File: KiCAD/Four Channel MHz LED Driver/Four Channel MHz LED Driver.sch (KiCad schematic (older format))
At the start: 15 parts

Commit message: Simpler power supply
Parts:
- removed C? (x2): 4.7uF, Capacitor_SMD:C_0805_2012Metric, symbol Device:C_Small
- removed C? (x3): 47uF, Capacitor_SMD:C_1206_3216Metric, symbol Device:C_Small
- removed C? (x2): 1uF, Capacitor_SMD:C_0603_1608Metric, symbol Device:C_Small
- removed C?: 100uF, Capacitor_SMD:C_1206_3216Metric, symbol Device:C_Small
- removed R? (x2): 100k, Resistor_SMD:R_0603_1608Metric, symbol Device:R_Small
- removed R?: 130k, Resistor_SMD:R_0603_1608Metric, symbol Device:R_Small
- removed R?: 60.4k, Resistor_SMD:R_0603_1608Metric, symbol Device:R_Small
- removed U?: LTM8049IY, LTM8049IY_ADI, symbol Custom_parts:LTM8049IY
- added C? (x4): 47uF, Capacitor_SMD:C_1206_3216Metric, symbol Device:C_Small
- added C? (x2): 1500pF, Capacitor_SMD:C_0603_1608Metric, symbol Device:C_Small
- added C? (x4): 2.2uF, Custom Footprints:0508_Capacitor, symbol Device:C_Small
- added L?: 10uH, Inductor_SMD:L_1210_3225Metric, symbol pspice:INDUCTOR
- added R?: 100, Resistor_SMD:R_0805_2012Metric, symbol Device:R_Small
- added U?: S18V20F12_12V_DC, symbol Custom_parts:S18V20F12_12V_DC
- added U?: DPBW06F-05, Custom Footprints:DPBW06F-05, symbol Custom_parts:DPBW06F-05
- added U?: ADP7118AUJZ-5.0-R7, Custom Footprints:ADP7118AUJZ-R7, symbol Custom_parts:ADP7118AUJZ-5.0-R7
- U?: footprint MUB10A_TEX -> Custom Footprints:DAC084S085CIMM
- U?: footprint TSSOP20_MC_MCH -> Custom Footprints:MCP4351-502E
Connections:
- net labels added: 5V-analog
- net labels removed: PS_Monitor
- wire segments 46 -> 54
- no-connect marks 5 -> 3
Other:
- note added: "ISOLATED - 12V to split +/- 5V"
- note added: "LDO - 12V to clean 5V for analog circuits"
- note added: "SEPIC - Vin (3V - 30V) to 12V DC"

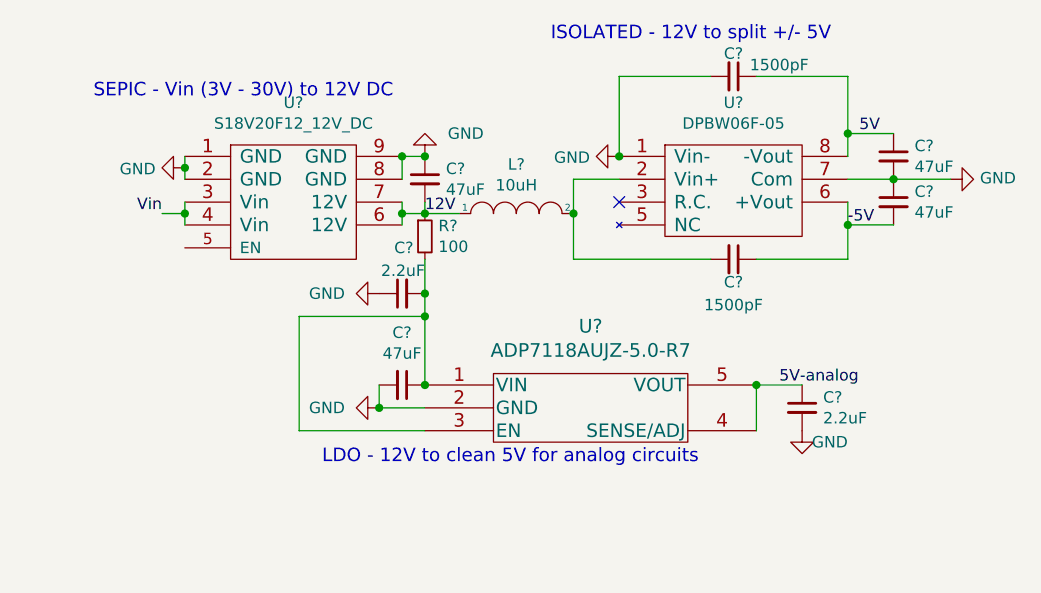
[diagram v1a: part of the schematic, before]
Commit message: Add Spice models
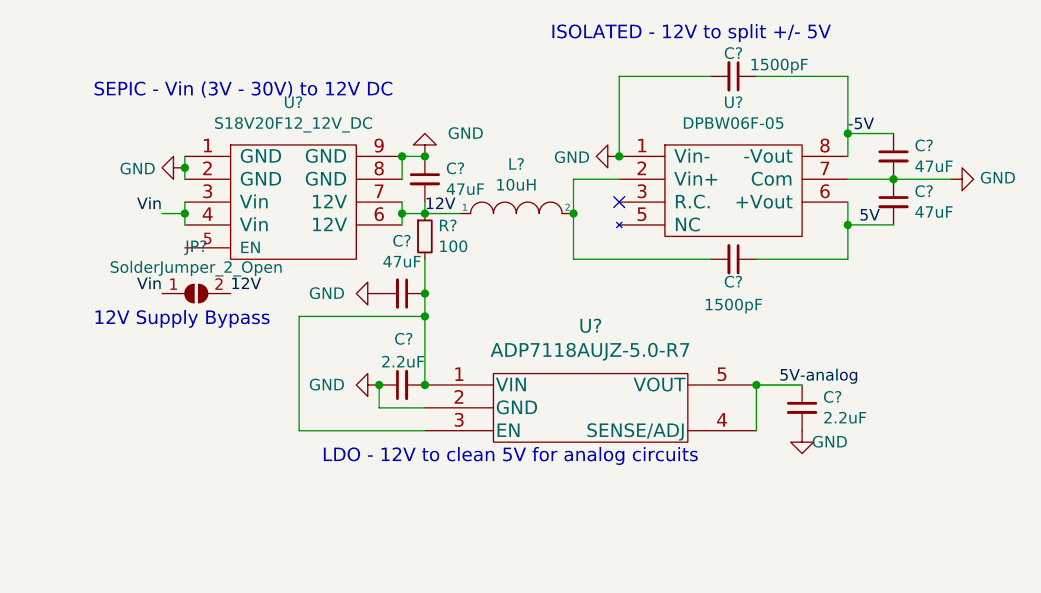
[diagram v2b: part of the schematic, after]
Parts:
- removed C?: 47uF, Capacitor_SMD:C_1206_3216Metric, symbol Device:C_Small
- added C?: 47uF, Capacitor_SMD:C_1206_3216Metric, symbol Device:C_Small
- added JP?: SolderJumper_2_Open, Jumper:SolderJumper-2_P1.3mm_Open_Pad1.0x1.5mm, symbol Jumper:SolderJumper_2_Open
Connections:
- net -5V: now also C?.1, C?.1, U?.8 (-Vout); no longer C?.1, C?.2, U?.6 (+Vout)
- net 12V: now also JP?.2 (B)
- net 5V: now also C?.1, C?.2, U?.6 (+Vout); no longer C?.1, C?.1, U?.8 (-Vout)
- net GND: now also C?.2
- net Vin: now also JP?.1 (A)
- net at C?.2, R?.2, U?.1 (VIN)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: now also C?.1
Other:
- note added: "12V Supply Bypass"
- moved on the sheet: C?
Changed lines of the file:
@@
 Wire Wire Line
 	5100 2050 5100 1950
-Text Label 5150 1650 0    50   ~ 0
+Text Label 5150 2050 0    50   ~ 0
 5V
-Text Label 5100 2050 0    50   ~ 0
+Text Label 5100 1650 0    50   ~ 0
 -5V
 Connection ~ 5300 1850
@@
 $EndComp
 $Comp
-L Device:C_Small C?
-U 1 1 5F37AFD2
-P 3150 2750
-F 0 "C?" V 2921 2750 50  0000 C CNN
-F 1 "47uF" V 3012 2750 50  0000 C CNN
-F 2 "Capacitor_SMD:C_1206_3216Metric" H 3150 2750 50  0001 C CNN
-F 3 "https://www.digikey.com/en/ptm/m/murata-electronics-north-america/high-cap-multilayer-ceramic-capacitors?pn_sku=490-16268-1-ND&part_id=7363259" H 3150 2750 50  0001 C CNN
-F 4 "Murata Electronics" H 3150 2750 50  0001 C CNN "Manufacturer"
-F 5 "GRM31CR61E476ME44L" H 3150 2750 50  0001 C CNN "Part #"
-	1    3150 2750
-	0    1    1    0
-$EndComp
-$Comp
 L Custom_parts:ADP7118AUJZ-5.0-R7 U?
 U 1 1 5F380EEB
@@
 	1    0    0    -1
 $EndComp
-$Comp
-L power:GND #PWR?
-U 1 1 5F3817B0
-P 3050 2850
-F 0 "#PWR?" H 3050 2600 50  0001 C CNN
-F 1 "GND" V 3050 2700 50  0000 R CNN
-F 2 "" H 3050 2850 50  0001 C CNN
-F 3 "" H 3050 2850 50  0001 C CNN
-	1    3050 2850
-	0    1    1    0
-$EndComp
 Connection ~ 3250 2750
-Wire Wire Line
-	3050 2750 3050 2850
-Wire Wire Line
-	3050 2850 3250 2850
-Connection ~ 3050 2850
-Wire Wire Line
-	2700 2950 3250 2950
 Wire Wire Line
 	4700 2950 4700 2750
@@
 L Device:C_Small C?
 U 1 1 5F38C930
-P 3150 2350
-F 0 "C?" V 3350 2300 50  0000 L CNN
-F 1 "2.2uF" V 3250 2250 50  0000 L CNN
-F 2 "Custom Footprints:0508_Capacitor" H 3150 2350 50  0001 C CNN
-F 3 "https://ds.yuden.co.jp/TYCOMPAS/ut/detail?pn=TWK212B7225MD-T%20&u=M" H 3150 2350 50  0001 C CNN
-F 4 "Taiyo Yuden" H 3150 2350 50  0001 C CNN "Manufacturer"
-F 5 "TWK212B7225MD-T" H 3150 2350 50  0001 C CNN "Part #"
-	1    3150 2350
+P 3150 2750
+F 0 "C?" V 3350 2700 50  0000 L CNN
+F 1 "2.2uF" V 3250 2650 50  0000 L CNN
+F 2 "Custom Footprints:0508_Capacitor" H 3150 2750 50  0001 C CNN
+F 3 "https://ds.yuden.co.jp/TYCOMPAS/ut/detail?pn=TWK212B7225MD-T%20&u=M" H 3150 2750 50  0001 C CNN
+F 4 "Taiyo Yuden" H 3150 2750 50  0001 C CNN "Manufacturer"
+F 5 "TWK212B7225MD-T" H 3150 2750 50  0001 C CNN "Part #"
+	1    3150 2750
 	0    -1   -1   0
 $EndComp
 Connection ~ 3250 2350
-Wire Wire Line
-	3250 2350 3250 2450
-Wire Wire Line
-	3250 2450 2700 2450
-Wire Wire Line
-	2700 2450 2700 2950
-Connection ~ 3250 2450
-Wire Wire Line
-	3250 2450 3250 2750
 $Comp
 L power:GND #PWR?
@@
 Text Notes 1800 1500 0    59   ~ 0
 SEPIC - Vin (3V - 30V) to 12V DC
+Wire Wire Line
+	3250 2350 3250 2450
+$Comp
+L Jumper:SolderJumper_2_Open JP?
+U 1 1 5F3A0F69
+P 2250 2350
+F 0 "JP?" H 2250 2555 50  0000 C CNN
+F 1 "SolderJumper_2_Open" H 2250 2464 50  0000 C CNN
+F 2 "Jumper:SolderJumper-2_P1.3mm_Open_Pad1.0x1.5mm" H 2250 2350 50  0001 C CNN
+F 3 "~" H 2250 2350 50  0001 C CNN
+	1    2250 2350
+	1    0    0    -1
+$EndComp
+Text Label 2100 2350 2    50   ~ 0
+Vin
+Text Label 2400 2350 0    50   ~ 0
+12V
+$Comp
+L Device:C_Small C?
+U 1 1 5F3A29AA
+P 3150 2350
+F 0 "C?" V 2921 2350 50  0000 C CNN
+F 1 "47uF" V 3012 2350 50  0000 C CNN
+F 2 "Capacitor_SMD:C_1206_3216Metric" H 3150 2350 50  0001 C CNN
+F 3 "https://www.digikey.com/en/ptm/m/murata-electronics-north-america/high-cap-multilayer-ceramic-capacitors?pn_sku=490-16268-1-ND&part_id=7363259" H 3150 2350 50  0001 C CNN
+F 4 "Murata Electronics" H 3150 2350 50  0001 C CNN "Manufacturer"
+F 5 "GRM31CR61E476ME44L" H 3150 2350 50  0001 C CNN "Part #"
+	1    3150 2350
+	0    1    1    0
+$EndComp
+Connection ~ 3250 2450
+Wire Wire Line
+	3250 2450 3250 2750
+$Comp
+L power:GND #PWR?
+U 1 1 5F3A55D8
+P 3050 2750
+F 0 "#PWR?" H 3050 2500 50  0001 C CNN
+F 1 "GND" V 3050 2600 50  0000 R CNN
+F 2 "" H 3050 2750 50  0001 C CNN
+F 3 "" H 3050 2750 50  0001 C CNN
+	1    3050 2750
+	0    1    1    0
+$EndComp
+Wire Wire Line
+	3050 2750 3050 2850
+Wire Wire Line
+	3050 2850 3250 2850
+Connection ~ 3050 2750
+Wire Wire Line
+	2700 2950 2700 2450
+Wire Wire Line
+	2700 2950 3250 2950
+Wire Wire Line
+	2700 2450 3250 2450
+Text Notes 1800 2500 0    59   ~ 0
+12V Supply Bypass
 $EndSCHEMATC

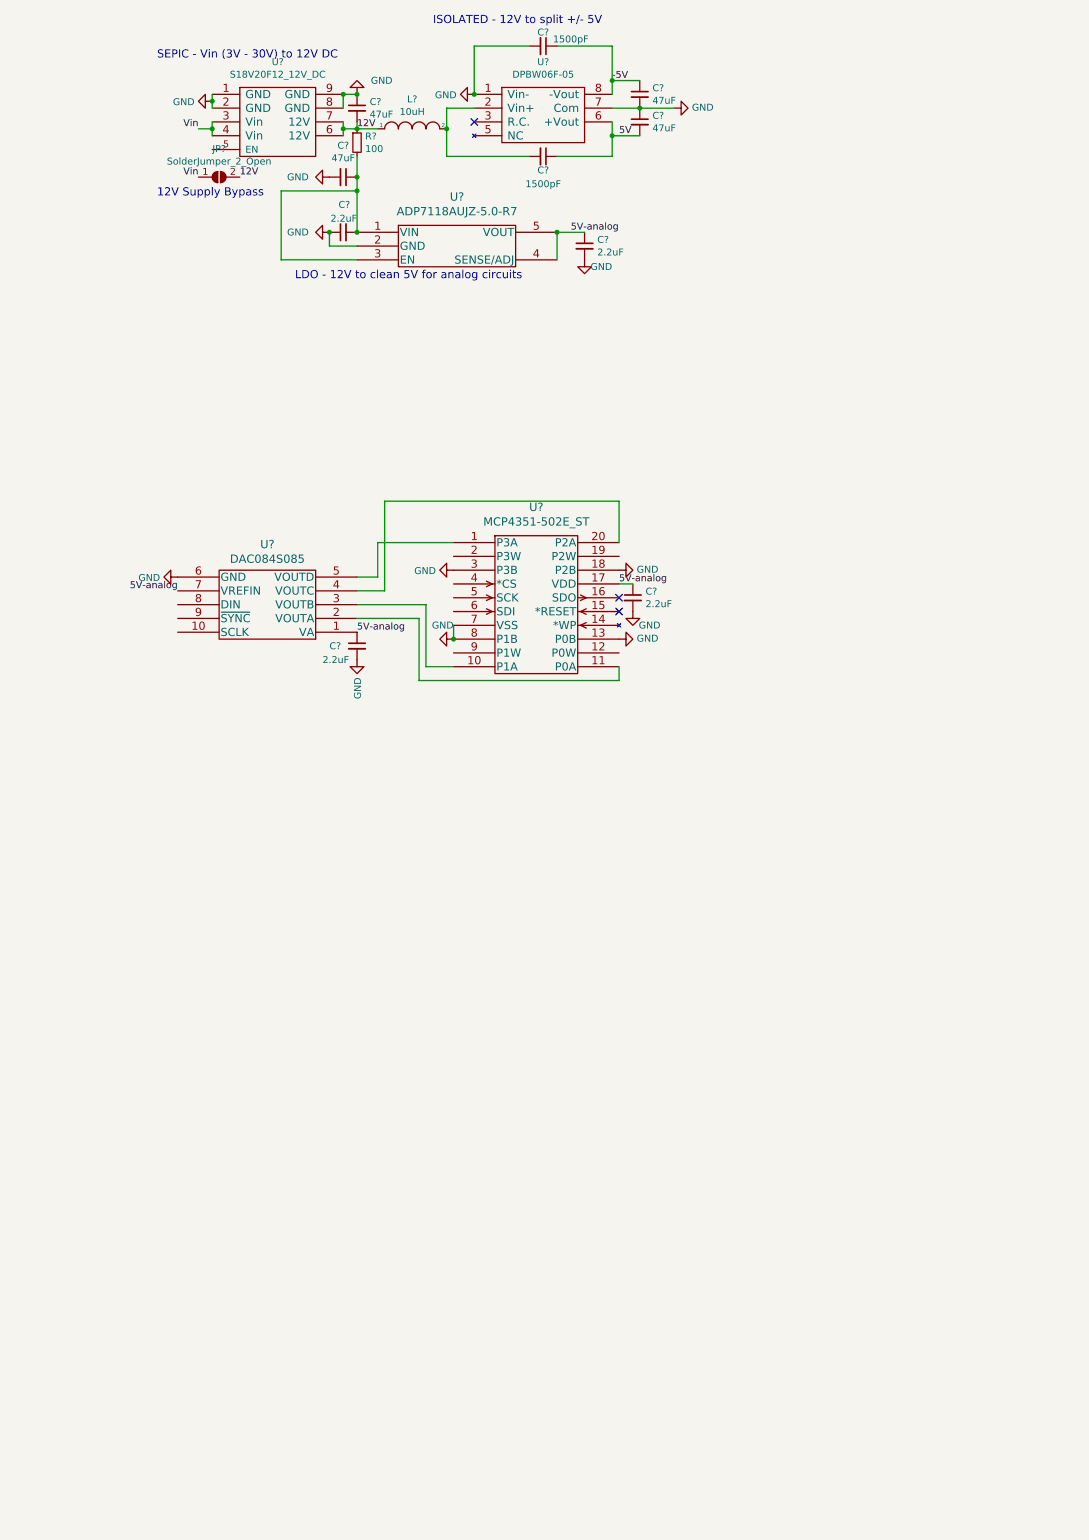
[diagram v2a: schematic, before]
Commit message: IO and IO clamps/protection added
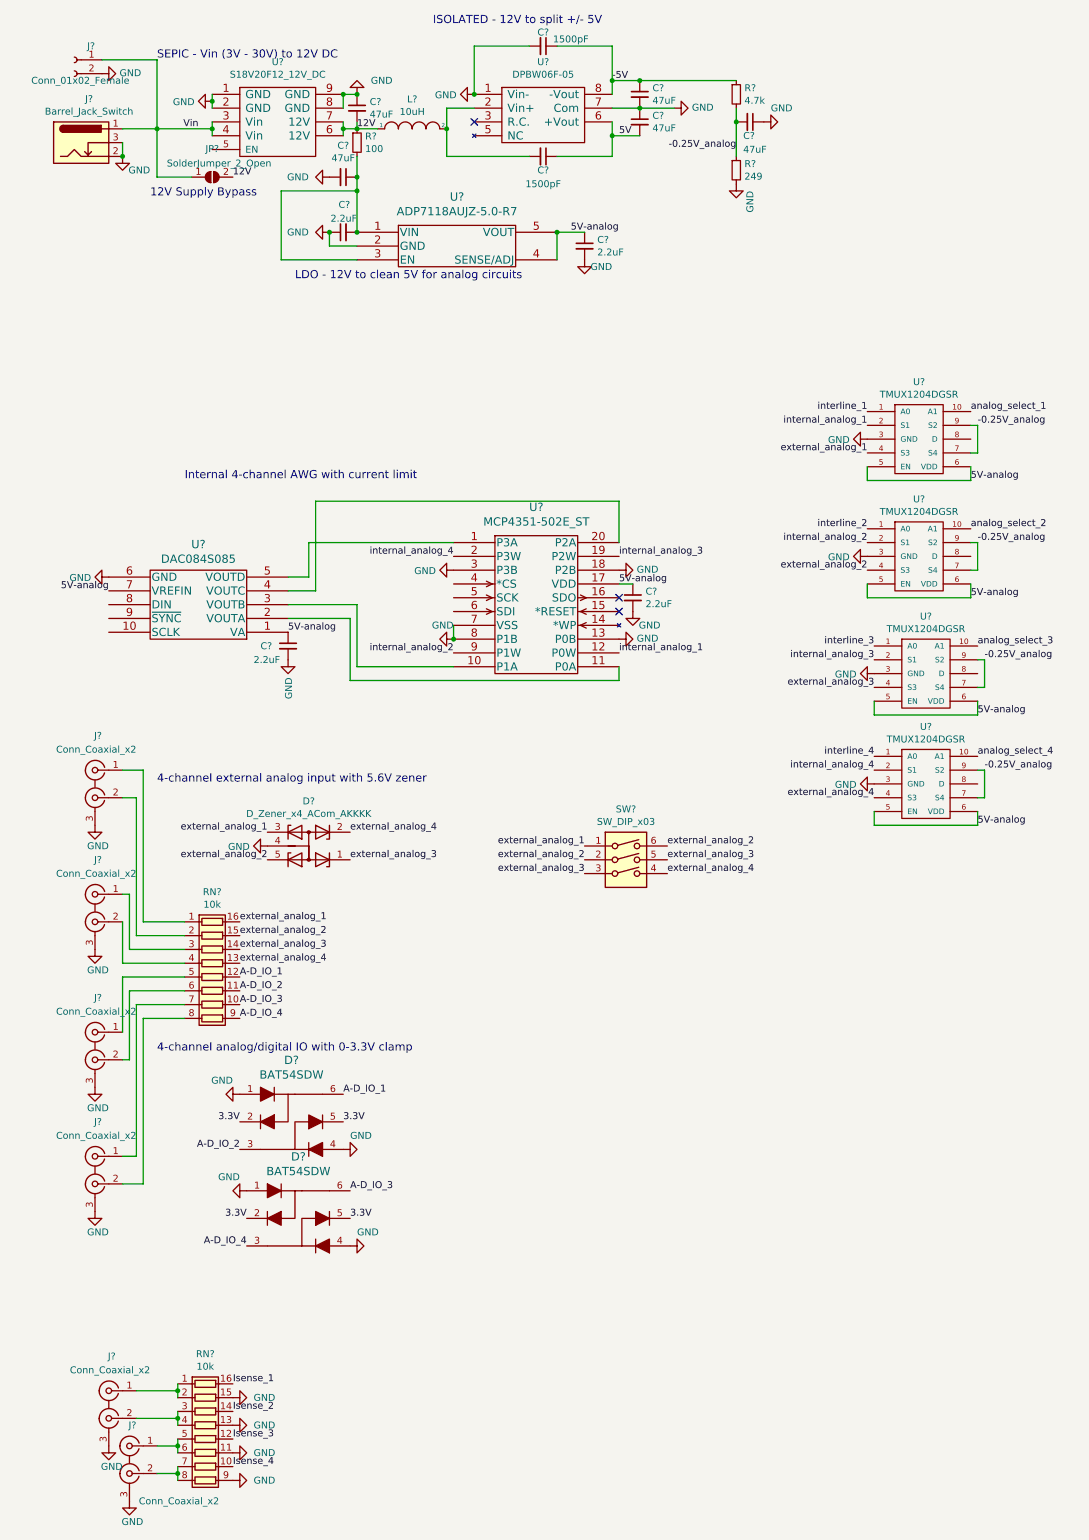
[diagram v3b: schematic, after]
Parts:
- added C?: 47uF, Capacitor_SMD:C_1206_3216Metric, symbol Device:C_Small
- added D? (x2): BAT54SDW, Package_TO_SOT_SMD:SOT-363_SC-70-6, symbol Custom_parts:BAT54SDW
- added D?: D_Zener_x4_ACom_AKKKK, Custom Footprints:SOT-753, symbol Custom_parts:D_Zener_x4_ACom_AKKKK
- added J? (x6): Conn_Coaxial_x2, Custom Footprints:031-6575_2x_BNC, symbol Connector:Conn_Coaxial_x2
- added J?: Barrel_Jack_Switch, Custom Footprints:54-00165-DC_Jack, symbol Connector:Barrel_Jack_Switch
- added J?: Conn_01x02_Female, Connector_Wire:SolderWire-2.5sqmm_1x02_P7.2mm_D2.4mm_OD3.6mm, symbol Connector:Conn_01x02_Female
- added R?: 4.7k, Resistor_SMD:R_0805_2012Metric, symbol Device:R_Small
- added R?: 249, Resistor_SMD:R_0603_1608Metric, symbol Device:R_Small
- added RN? (x2): 10k, Custom Footprints:Bourns_16-SOIC_8x_r-pack, symbol Device:R_Pack08
- added SW?: SW_DIP_x03, Custom Footprints:SW_DS04-254-2-03BK-SMT, symbol Switch:SW_DIP_x03
- added U? (x4): TMUX1204DGSR, Custom Footprints:TMUX1204DGSR, symbol Custom_parts:TMUX1204DGSR
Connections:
- net -5V: now also R?.1
- net 5V-analog: now also U?.5 (EN), U?.5 (EN), U?.5 (EN), U?.5 (EN), U?.6 (VDD), U?.6 (VDD), U?.6 (VDD), U?.6 (VDD)
- net GND: now also C?.1, D?.1, D?.1, D?.4, D?.4, D?.4 (A), J?.2, J?.2 (Pin_2), J?.3, J?.3 (EXT), J?.3 (EXT), J?.3 (EXT), J?.3 (EXT), J?.3 (EXT), J?.3 (EXT), R?.2, RN?.11 (R6.2), RN?.13 (R4.2), RN?.15 (R2.2), RN?.9 (R8.2), U?.3 (GND), U?.3 (GND), U?.3 (GND), U?.3 (GND)
- net Vin: now also J?.1, J?.1 (Pin_1)
- net internal_analog_1: now reaches U?.12 (P0W)
- net internal_analog_1: now also U?.2 (S1)
- net internal_analog_3: now reaches U?.19 (P2W)
- net internal_analog_3: now also U?.2 (S1)
- net internal_analog_4: now reaches U?.2 (P3W)
- net internal_analog_4: now also U?.2 (S1)
- net internal_analog_2: now reaches U?.9 (P1W)
- net internal_analog_2: now also U?.2 (S1)
- new net: J?.1 (IN1), RN?.3 (R3.1)
- new net: J?.2 (IN2), RN?.4 (R4.1)
- new net: J?.1 (IN1), RN?.1 (R1.1)
- new net: J?.2 (IN2), RN?.2 (R2.1)
- new net: J?.1 (IN1), RN?.7 (R7.1)
- new net: J?.2 (IN2), RN?.8 (R8.1)
- new net: J?.1 (IN1), RN?.5 (R5.1)
- new net: J?.2 (IN2), RN?.6 (R6.1)
- new net: J?.1 (IN1), RN?.1 (R1.1), RN?.2 (R2.1)
- new net: J?.2 (IN2), RN?.3 (R3.1), RN?.4 (R4.1)
- new net: J?.1 (IN1), RN?.5 (R5.1), RN?.6 (R6.1)
- new net: J?.2 (IN2), RN?.7 (R7.1), RN?.8 (R8.1)
- new net -0.25V_analog: C?.2, R?.1, R?.2, U?.7 (S4), U?.7 (S4), U?.7 (S4), U?.7 (S4), U?.9 (S2), U?.9 (S2), U?.9 (S2), U?.9 (S2)
- new net 3.3V: D?.2, D?.2, D?.5, D?.5
- new net A-D_IO_1: D?.6, RN?.12 (R5.2)
- new net A-D_IO_2: D?.3, RN?.11 (R6.2)
- new net A-D_IO_3: D?.6, RN?.10 (R7.2)
- new net A-D_IO_4: D?.3, RN?.9 (R8.2)
- new net Isense_1: RN?.16 (R1.2)
- new net Isense_2: RN?.14 (R3.2)
- new net Isense_3: RN?.12 (R5.2)
- new net Isense_4: RN?.10 (R7.2)
- new net analog_select_1: U?.10 (A1)
- new net analog_select_2: U?.10 (A1)
- new net analog_select_3: U?.10 (A1)
- new net analog_select_4: U?.10 (A1)
- new net external_analog_1: D?.3 (K), RN?.16 (R1.2), SW?.1, U?.4 (S3)
- new net external_analog_2: D?.5 (K), RN?.15 (R2.2), SW?.2, SW?.6, U?.4 (S3)
- new net external_analog_3: D?.1 (K), RN?.14 (R3.2), SW?.3, SW?.5, U?.4 (S3)
- new net external_analog_4: D?.2 (K), RN?.13 (R4.2), SW?.4, U?.4 (S3)
- new net interline_1: U?.1 (A0)
- new net interline_2: U?.1 (A0)
- new net interline_3: U?.1 (A0)
- new net interline_4: U?.1 (A0)
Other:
- note added: "4-channel analog/digital IO with 0-3.3V clamp"
- note added: "4-channel external analog input with 5.6V zener"
- note added: "Internal 4-channel AWG with current limit"
- moved on the sheet: C?, JP?, U?
